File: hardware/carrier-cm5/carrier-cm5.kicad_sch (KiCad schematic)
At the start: 8 parts

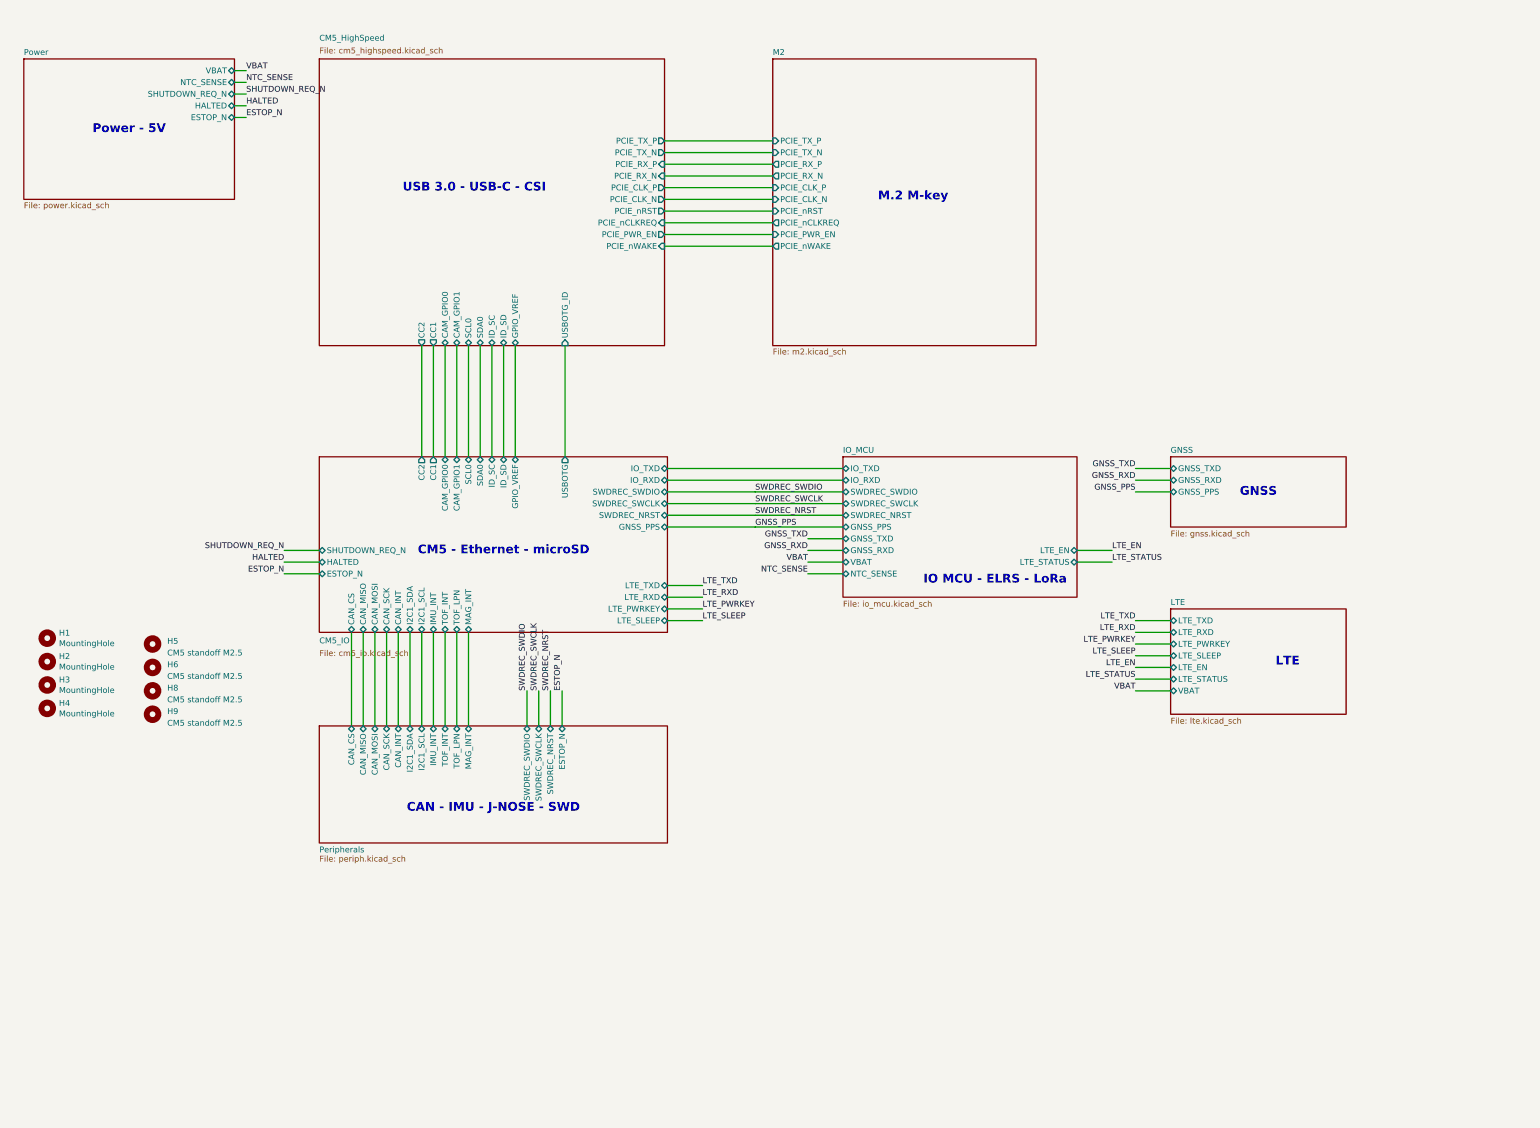
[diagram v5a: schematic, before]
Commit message: Updated schematic on CM5 carrier
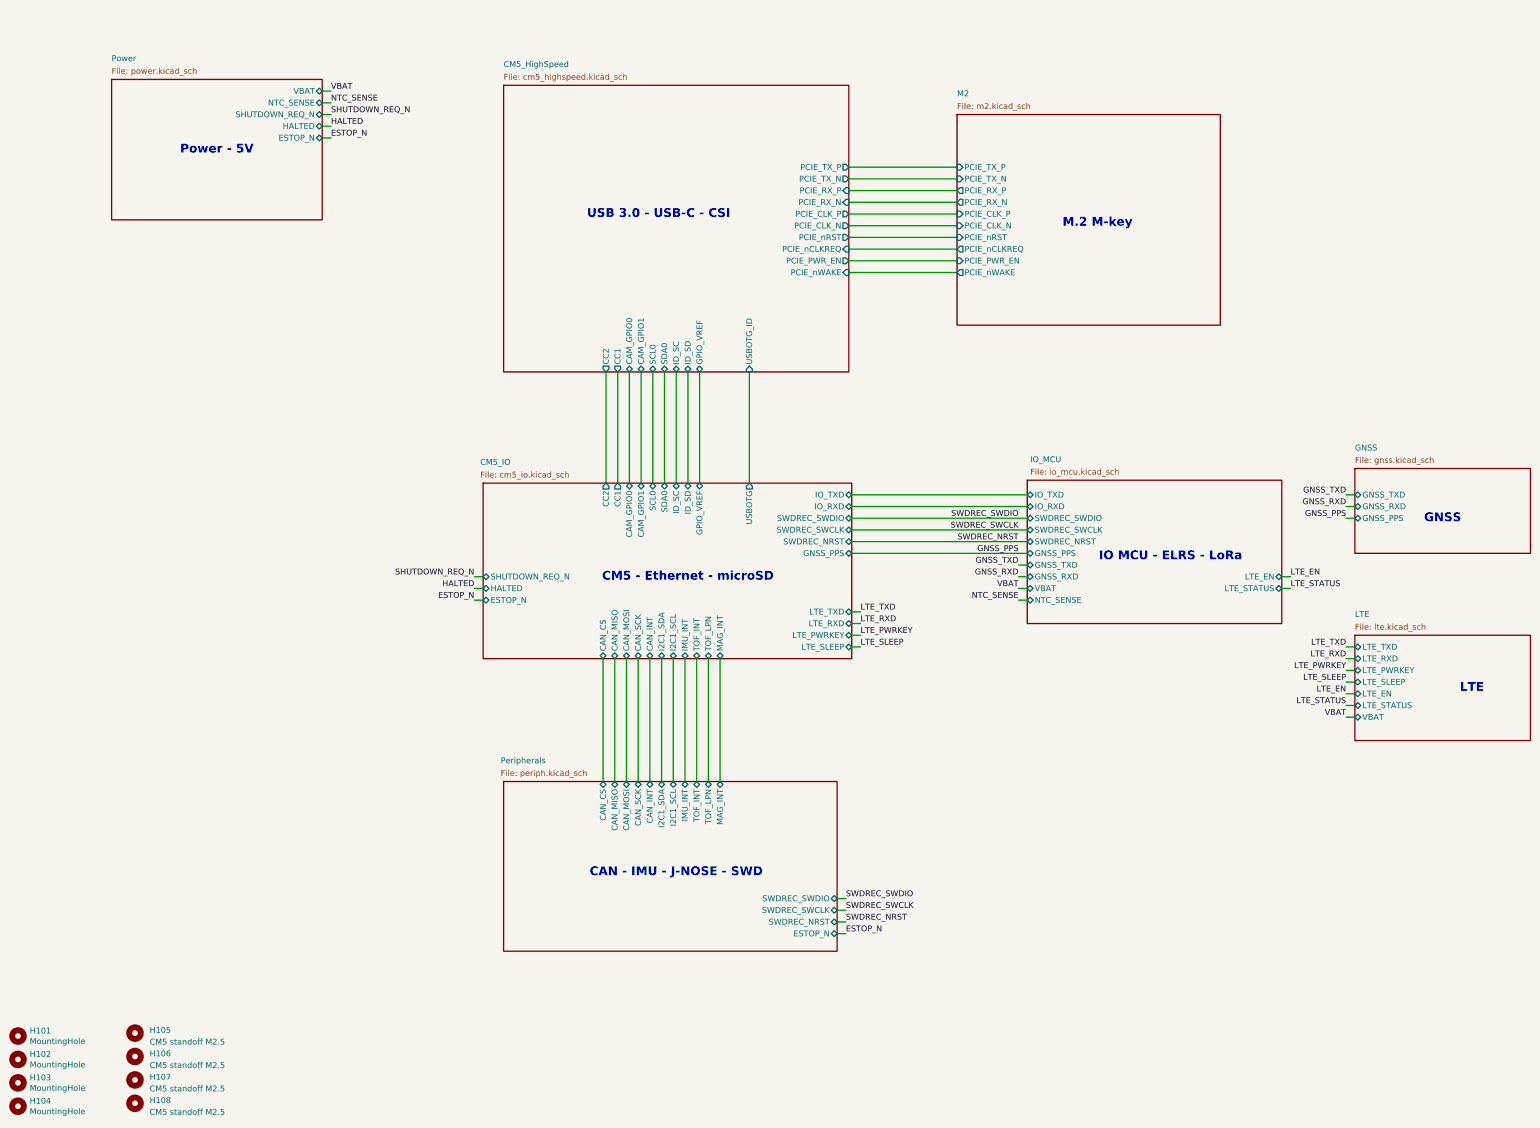
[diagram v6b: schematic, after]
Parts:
- renumbered H1 to H101, H2 to H102, H3 to H103, H4 to H104, H5 to H105, H6 to H106, H8 to H107, H9 to H108
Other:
- company: AAC -> (none)
- moved on the sheet: H101, H102, H103, H104, H105, H106, H107, H108
